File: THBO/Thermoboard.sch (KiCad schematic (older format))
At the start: 41 parts, among them P101 CONN_01X02, P102 CONN_02X08, P103 CONN_01X02, P104 CONN_02X08, P105 CONN_01X02, P106 CONN_01X02, P107 CONN_01X02, P108 CONN_01X02, P109 CONN_01X02, P110 CONN_01X02, P111 CONN_01X02, P112 CONN_01X02, P113 CONN_01X02, P114 CONN_01X02, P115 CONN_01X02, P116 CONN_01X02, P117 CONN_01X02, P118 CONN_01X02, P119 CONN_01X02, P120 CONN_01X02, P121 CONN_01X02, P122 CONN_01X02, P123 CONN_01X02, P124 CONN_01X02, P125 CONN_01X02, P126 CONN_01X02, P127 CONN_01X02, P128 CONN_01X02, P129 CONN_01X02, P130 CONN_01X02, P131 CONN_01X02, P132 CONN_01X02, P133 CONN_01X02, P134 CONN_01X02, P135 CONN_01X02, U101 OPA380

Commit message: Updated THBO to Rev2
-Split the board into two parts to allow for better placement on the
pod.
-Added LEDs to 5V line
-Added pin headers at the input terminals to easily put the board into
self-reference mode using jumpers
-Changed Vref from 0.64V to 1.25V
-Updated schematic to modular design
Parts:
- added C103: 1uF, Capacitors_SMD:C_1206_HandSoldering, symbol C
- added C104: SAT, Resistors_SMD:R_1206_HandSoldering, symbol C
- added D101, D102: GREEN, LEDs:LED_1206, symbol LED
- added J101, J102, J103, J104, J105, J106, J107, J108, J109, J110, J111, J112, J113, J114, J115, J116, J117, J118, J119, J120, J121, J122, J123, J124, J125, J126, J127, J128, J129, J130, J131, J132: CONN_02X02, Pin_Headers:Pin_Header_Straight_2x02_Pitch2.54mm, symbol CONN_02X02
- added J133, J134, J135, J136: MOUNTING_HOLE, hyperCustom:MountingHole_5.5mm_Pad_Via, symbol MOUNTING_HOLE
- added P136: CONN_01X02, thermoFootprints:phoenix_2pin_3.5mm, symbol CONN_01X02
- added R104: 3k, Resistors_SMD:R_1206_HandSoldering, symbol R
- added R105: 1k, Resistors_SMD:R_1206_HandSoldering, symbol R
- added R106: 0, Resistors_SMD:R_1206_HandSoldering, symbol R
- added R107, R108: 300, SMD_Packages:SMD-1206_Pol, symbol R
- added U102: OPA380, Housings_SSOP:MSOP-8_3x3mm_Pitch0.65mm, symbol OPA380
- R101: value R -> 3k; Digikey P/N RHM1.00KYCT-ND -> 408-1910-1-ND; Mfg. (none) -> Susumu; Mfg. P/N (none) -> HRG3216P-3001-D-T1
- R102: value R -> 1k; Digikey P/N 408-1814-1-ND -> 408-1806-1-ND; Mfg. (none) -> Susumu; Mfg. P/N (none) -> PRG3216P-1001-D-T5
- R103: value 10 -> 0; Digikey P/N RCL10DCT-ND -> 749-1062-1-ND; Mfg. (none) -> Vishay Dale; Mfg. P/N (none) -> RCA06120000Z0EALS
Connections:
- net GND: now also C103.1, C104.2, D101.1 (K), D102.1 (K), J101.2 (P2), J101.3 (P3), J102.2 (P2), J102.3 (P3), J103.2 (P2), J103.3 (P3), J104.2 (P2), J104.3 (P3), J105.2 (P2), J105.3 (P3), J106.2 (P2), J106.3 (P3), J107.2 (P2), J107.3 (P3), J108.2 (P2), J108.3 (P3), J109.2 (P2), J109.3 (P3), J110.2 (P2), J110.3 (P3), J111.2 (P2), J111.3 (P3), J112.2 (P2), J112.3 (P3), J113.2 (P2), J113.3 (P3), J114.2 (P2), J114.3 (P3), J115.2 (P2), J115.3 (P3), J116.2 (P2), J116.3 (P3), J117.2 (P2), J117.3 (P3), J118.2 (P2), J118.3 (P3), J119.2 (P2), J119.3 (P3), J120.2 (P2), J120.3 (P3), J121.2 (P2), J121.3 (P3), J122.2 (P2), J122.3 (P3), J123.2 (P2), J123.3 (P3), J124.2 (P2), J124.3 (P3), J125.2 (P2), J125.3 (P3), J126.2 (P2), J126.3 (P3), J127.2 (P2), J127.3 (P3), J128.2 (P2), J128.3 (P3), J129.2 (P2), J129.3 (P3), J130.2 (P2), J130.3 (P3), J131.2 (P2), J131.3 (P3), J132.2 (P2), J132.3 (P3), J133.1, J134.1, J135.1, J136.1, P136.2 (P2), R105.2, U102.4 (V-)
- net +5V renamed +5V_L
- net +5V_L: now also R107.1
- net Vref renamed Vref_L
- net sheet58677ED1/+IN renamed Thermocouple Amplifier -- 2/+IN
- net Thermocouple Amplifier -- 2/+IN: now also J102.4 (P4)
- net sheet58677ED1/-IN renamed Thermocouple Amplifier -- 2/-IN
- net Thermocouple Amplifier -- 2/-IN: now also J102.1 (P1)
- net sheet58677ED1/OUT renamed THERMO_OUPUT_2
- net sheet58677FA8/+IN renamed Thermocouple Amplifier -- 3/+IN
- net Thermocouple Amplifier -- 3/+IN: now also J103.4 (P4)
- net sheet58677FA8/-IN renamed Thermocouple Amplifier -- 3/-IN
- net Thermocouple Amplifier -- 3/-IN: now also J103.1 (P1)
- net sheet58677FA8/OUT renamed THERMO_OUPUT_3
- net sheet58678359/+IN renamed Thermocouple Amplifier -- 4/+IN
- net Thermocouple Amplifier -- 4/+IN: now also J104.4 (P4)
- net sheet58678359/-IN renamed Thermocouple Amplifier -- 4/-IN
- net Thermocouple Amplifier -- 4/-IN: now also J104.1 (P1)
- net sheet58678359/OUT renamed THERMO_OUPUT_4
- net sheet58678C44/+IN renamed Thermocouple Amplifier -- 5/+IN
- net Thermocouple Amplifier -- 5/+IN: now also J105.4 (P4)
- net sheet58678C44/-IN renamed Thermocouple Amplifier -- 5/-IN
- net Thermocouple Amplifier -- 5/-IN: now also J105.1 (P1)
- net sheet58678C44/OUT renamed THERMO_OUPUT_5
- net sheet58678C45/+IN renamed Thermocouple Amplifier -- 6/+IN
- net Thermocouple Amplifier -- 6/+IN: now also J106.4 (P4)
- net sheet58678C45/-IN renamed Thermocouple Amplifier -- 6/-IN
- net Thermocouple Amplifier -- 6/-IN: now also J106.1 (P1)
- net sheet58678C45/OUT renamed THERMO_OUPUT_6
- net sheet58678C46/+IN renamed Thermocouple Amplifier -- 7/+IN
- net Thermocouple Amplifier -- 7/+IN: now also J107.4 (P4)
- net sheet58678C46/-IN renamed Thermocouple Amplifier -- 7/-IN
- net Thermocouple Amplifier -- 7/-IN: now also J107.1 (P1)
- net sheet58678C46/OUT renamed THERMO_OUPUT_7
- net sheet58678C47/+IN renamed Thermocouple Amplifier -- 8/+IN
- net Thermocouple Amplifier -- 8/+IN: now also J108.4 (P4)
- net sheet58678C47/-IN renamed Thermocouple Amplifier -- 8/-IN
- net Thermocouple Amplifier -- 8/-IN: now also J108.1 (P1)
- net sheet58678C47/OUT renamed THERMO_OUPUT_8
- net sheet586796DF/+IN renamed Thermocouple Amplifier -- 1/+IN
- net Thermocouple Amplifier -- 1/+IN: now also J101.4 (P4)
- net sheet586796DF/-IN renamed Thermocouple Amplifier -- 1/-IN
- net Thermocouple Amplifier -- 1/-IN: now also J101.1 (P1)
- net sheet586796DF/OUT renamed THERMO_OUPUT_1
- net sheet5867A098/+IN renamed Thermocouple Amplifier -- 9/+IN
- net Thermocouple Amplifier -- 9/+IN: now also J109.4 (P4)
- net sheet5867A098/-IN renamed Thermocouple Amplifier -- 9/-IN
- net Thermocouple Amplifier -- 9/-IN: now also J109.1 (P1)
- net sheet5867A098/OUT renamed THERMO_OUPUT_9
- net sheet5867A099/+IN renamed Thermocouple Amplifier -- 10/+IN
- net Thermocouple Amplifier -- 10/+IN: now also J110.4 (P4)
- net sheet5867A099/-IN renamed Thermocouple Amplifier -- 10/-IN
- net Thermocouple Amplifier -- 10/-IN: now also J110.1 (P1)
- net sheet5867A099/OUT renamed THERMO_OUPUT_10
- net sheet5867A09A/+IN renamed Thermocouple Amplifier -- 11/+IN
- net Thermocouple Amplifier -- 11/+IN: now also J111.4 (P4)
- net sheet5867A09A/-IN renamed Thermocouple Amplifier -- 11/-IN
- net Thermocouple Amplifier -- 11/-IN: now also J111.1 (P1)
- net sheet5867A09A/OUT renamed THERMO_OUPUT_11
- net sheet5867A09B/+IN renamed Thermocouple Amplifier -- 12/+IN
- net Thermocouple Amplifier -- 12/+IN: now also J112.4 (P4)
- net sheet5867A09B/-IN renamed Thermocouple Amplifier -- 12/-IN
- net Thermocouple Amplifier -- 12/-IN: now also J112.1 (P1)
- net sheet5867A09B/OUT renamed THERMO_OUPUT_12
- net sheet5867B428/+IN renamed Thermocouple Amplifier -- 13/+IN
- net Thermocouple Amplifier -- 13/+IN: now also J113.4 (P4)
- net sheet5867B428/-IN renamed Thermocouple Amplifier -- 13/-IN
- net Thermocouple Amplifier -- 13/-IN: now also J113.1 (P1)
- net sheet5867B428/OUT renamed THERMO_OUPUT_13
- net sheet5867B429/+IN renamed Thermocouple Amplifier -- 14/+IN
- net Thermocouple Amplifier -- 14/+IN: now also J114.4 (P4)
- net sheet5867B429/-IN renamed Thermocouple Amplifier -- 14/-IN
- net Thermocouple Amplifier -- 14/-IN: now also J114.1 (P1)
- net sheet5867B429/OUT renamed THERMO_OUPUT_14
- net sheet5867B42A/+IN renamed Thermocouple Amplifier -- 15/+IN
- net Thermocouple Amplifier -- 15/+IN: now also J115.4 (P4)
- net sheet5867B42A/-IN renamed Thermocouple Amplifier -- 15/-IN
- net Thermocouple Amplifier -- 15/-IN: now also J115.1 (P1)
- net sheet5867B42A/OUT renamed THERMO_OUPUT_15
- net sheet5867B42B/+IN renamed Thermocouple Amplifier -- 16/+IN
- net Thermocouple Amplifier -- 16/+IN: now also J116.4 (P4)
- net sheet5867B42B/-IN renamed Thermocouple Amplifier -- 16/-IN
- net Thermocouple Amplifier -- 16/-IN: now also J116.1 (P1)
- net sheet5867B42B/OUT renamed THERMO_OUPUT_16
- net sheet5868210E/+IN renamed Thermocouple Amplifier -- 17/+IN
- net Thermocouple Amplifier -- 17/+IN: now also J117.4 (P4)
- net sheet5868210E/-IN renamed Thermocouple Amplifier -- 17/-IN
- net Thermocouple Amplifier -- 17/-IN: now also J117.1 (P1)
- net sheet5868210E/OUT renamed THERMO_OUPUT_17
- net sheet5868210F/+IN renamed Thermocouple Amplifier -- 18/+IN
- net Thermocouple Amplifier -- 18/+IN: now also J118.4 (P4)
- net sheet5868210F/-IN renamed Thermocouple Amplifier -- 18/-IN
- net Thermocouple Amplifier -- 18/-IN: now also J118.1 (P1)
- net sheet5868210F/OUT renamed THERMO_OUPUT_18
- net sheet58682110/+IN renamed Thermocouple Amplifier -- 19/+IN
- net Thermocouple Amplifier -- 19/+IN: now also J119.4 (P4)
- net sheet58682110/-IN renamed Thermocouple Amplifier -- 19/-IN
- net Thermocouple Amplifier -- 19/-IN: now also J119.1 (P1)
- net sheet58682110/OUT renamed THERMO_OUPUT_19
- net sheet58682111/+IN renamed Thermocouple Amplifier -- 20/+IN
- net Thermocouple Amplifier -- 20/+IN: now also J120.4 (P4)
- net sheet58682111/-IN renamed Thermocouple Amplifier -- 20/-IN
- net Thermocouple Amplifier -- 20/-IN: now also J120.1 (P1)
- net sheet58682111/OUT renamed THERMO_OUPUT_20
- net sheet58682112/+IN renamed Thermocouple Amplifier -- 21/+IN
- net Thermocouple Amplifier -- 21/+IN: now also J121.4 (P4)
- net sheet58682112/-IN renamed Thermocouple Amplifier -- 21/-IN
- net Thermocouple Amplifier -- 21/-IN: now also J121.1 (P1)
- net sheet58682112/OUT renamed THERMO_OUPUT_21
- net sheet58682113/+IN renamed Thermocouple Amplifier -- 22/+IN
- net Thermocouple Amplifier -- 22/+IN: now also J122.4 (P4)
- net sheet58682113/-IN renamed Thermocouple Amplifier -- 22/-IN
- net Thermocouple Amplifier -- 22/-IN: now also J122.1 (P1)
- net sheet58682113/OUT renamed THERMO_OUPUT_22
- net sheet58682114/+IN renamed Thermocouple Amplifier -- 23/+IN
- net Thermocouple Amplifier -- 23/+IN: now also J123.4 (P4)
- net sheet58682114/-IN renamed Thermocouple Amplifier -- 23/-IN
- net Thermocouple Amplifier -- 23/-IN: now also J123.1 (P1)
- net sheet58682114/OUT renamed THERMO_OUPUT_23
- net sheet58682115/+IN renamed Thermocouple Amplifier -- 24/+IN
- net Thermocouple Amplifier -- 24/+IN: now also J124.4 (P4)
- net sheet58682115/-IN renamed Thermocouple Amplifier -- 24/-IN
- net Thermocouple Amplifier -- 24/-IN: now also J124.1 (P1)
- net sheet58682115/OUT renamed THERMO_OUPUT_24
- net sheet58682116/+IN renamed Thermocouple Amplifier -- 25/+IN
- net Thermocouple Amplifier -- 25/+IN: now also J125.4 (P4)
- net sheet58682116/-IN renamed Thermocouple Amplifier -- 25/-IN
- net Thermocouple Amplifier -- 25/-IN: now also J125.1 (P1)
- net sheet58682116/OUT renamed THERMO_OUPUT_25
- net sheet58682117/+IN renamed Thermocouple Amplifier -- 26/+IN
- net Thermocouple Amplifier -- 26/+IN: now also J126.4 (P4)
- net sheet58682117/-IN renamed Thermocouple Amplifier -- 26/-IN
- net Thermocouple Amplifier -- 26/-IN: now also J126.1 (P1)
- net sheet58682117/OUT renamed THERMO_OUPUT_26
- net sheet58682118/+IN renamed Thermocouple Amplifier -- 27/+IN
- net Thermocouple Amplifier -- 27/+IN: now also J127.4 (P4)
- net sheet58682118/-IN renamed Thermocouple Amplifier -- 27/-IN
- net Thermocouple Amplifier -- 27/-IN: now also J127.1 (P1)
- net sheet58682118/OUT renamed THERMO_OUPUT_27
- net sheet58682119/+IN renamed Thermocouple Amplifier -- 28/+IN
- net Thermocouple Amplifier -- 28/+IN: now also J128.4 (P4)
- net sheet58682119/-IN renamed Thermocouple Amplifier -- 28/-IN
- net Thermocouple Amplifier -- 28/-IN: now also J128.1 (P1)
- net sheet58682119/OUT renamed THERMO_OUPUT_28
- net sheet5868211A/+IN renamed Thermocouple Amplifier -- 29/+IN
- net Thermocouple Amplifier -- 29/+IN: now also J129.4 (P4)
- net sheet5868211A/-IN renamed Thermocouple Amplifier -- 29/-IN
- net Thermocouple Amplifier -- 29/-IN: now also J129.1 (P1)
- net sheet5868211A/OUT renamed THERMO_OUPUT_29
- net sheet5868211B/+IN renamed Thermocouple Amplifier -- 30/+IN
- net Thermocouple Amplifier -- 30/+IN: now also J130.4 (P4)
- net sheet5868211B/-IN renamed Thermocouple Amplifier -- 30/-IN
- net Thermocouple Amplifier -- 30/-IN: now also J130.1 (P1)
- net sheet5868211B/OUT renamed THERMO_OUPUT_30
- net sheet5868211C/+IN renamed Thermocouple Amplifier -- 31/+IN
- net Thermocouple Amplifier -- 31/+IN: now also J131.4 (P4)
- net sheet5868211C/-IN renamed Thermocouple Amplifier -- 31/-IN
- net Thermocouple Amplifier -- 31/-IN: now also J131.1 (P1)
- net sheet5868211C/OUT renamed THERMO_OUPUT_31
- net sheet5868211D/+IN renamed Thermocouple Amplifier -- 32/+IN
- net Thermocouple Amplifier -- 32/+IN: now also J132.4 (P4)
- net sheet5868211D/-IN renamed Thermocouple Amplifier -- 32/-IN
- net Thermocouple Amplifier -- 32/-IN: now also J132.1 (P1)
- net sheet5868211D/OUT renamed THERMO_OUPUT_32
- new net: R104.2, R105.1, U102.3 (+In)
- new net: D101.2 (A), R107.2
- new net: D102.2 (A), R108.2
- new net: R106.2, U102.2 (-In), U102.6 (Out)
- new net +5V_R: C103.2, P136.1 (P1), R104.1, R108.1, U102.7 (V+)
- new net Vref_R: C104.1, R106.1
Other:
- note added: "Mounting Holes"
- note added: "Power Input and Voltage Reference"
- note added: "Thermoboard (LEFT)"
- note added: "Thermoboard (RIGHT)"
- note added: "Thermocouple Amplifiers"
- note added: "Vref = 1.25V"
- note removed: "EXTRA/\nSPARE\n\n"
- moved on the sheet: C101, C102, P101, P102, P103, R101, R102, R103, U101

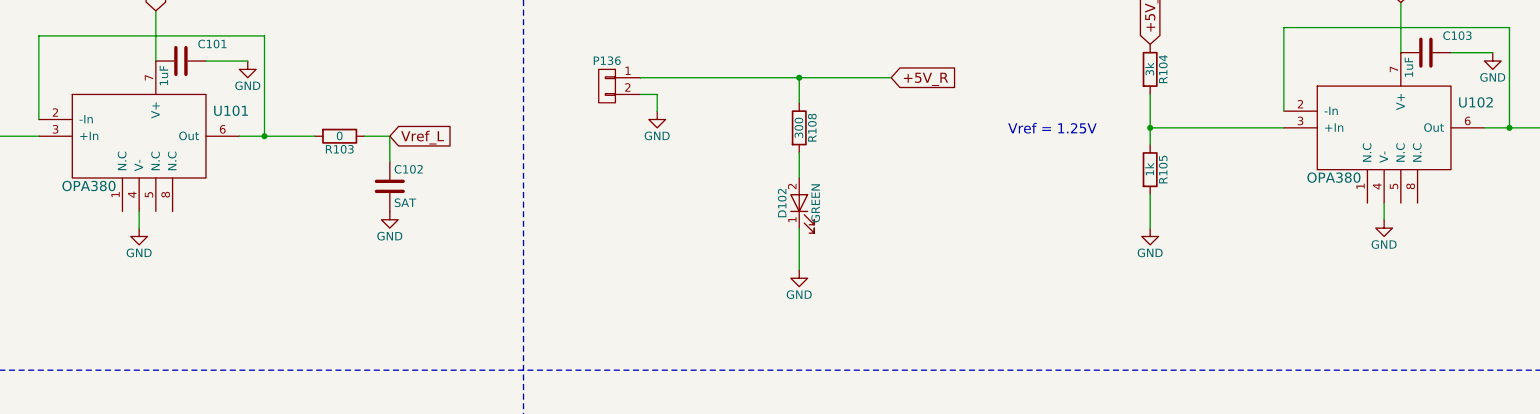
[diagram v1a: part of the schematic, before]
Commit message: Converted back to 8 24V rails on MPB, fixed NC pins on THBO schematic
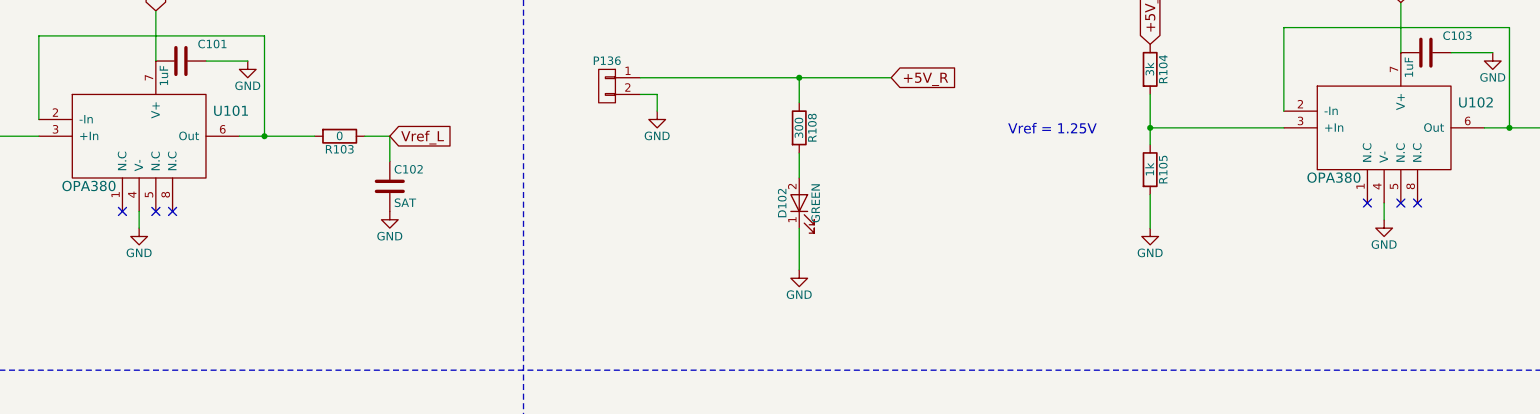
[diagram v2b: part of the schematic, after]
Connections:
- no-connect marks 0 -> 6
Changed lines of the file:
@@
 $EndComp
 Connection ~ 3450 21800
+NoConn ~ 5200 4350
+NoConn ~ 5400 4350
+NoConn ~ 5500 4350
+NoConn ~ 12650 4300
+NoConn ~ 12850 4300
+NoConn ~ 12950 4300
 $EndSCHEMATC

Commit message: THBO BOM Update, MPB GPIO Schematic
THBO
- Updated a few componets parameter values for BOM
- Created BOM for the board

MPB
- Created Schematic for GPIO Circuit to control regulators
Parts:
- D101, D102: DigiKey PN 754-1944-1-ND -> (none); Digikey P/N (none) -> 754-1944-1-ND; Mfg. P/N (none) -> APT3216LZGCK; Mfg. PN APT3216LZGCK -> (none)
- J101: Digikey P/N (none) -> 609-3242-ND; Mfg. (none) -> Amphenol FCI; Mfg. P/N (none) -> 67997-404HLF
- R107, R108: DigiKey PN P300ALCT-ND -> (none); Digikey P/N (none) -> P300ALCT-ND; Mfg. P/N (none) -> ERJ-P08J301V; Mfg. PN ERJ-P08J301V -> (none)
